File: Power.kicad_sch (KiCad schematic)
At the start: 11 parts

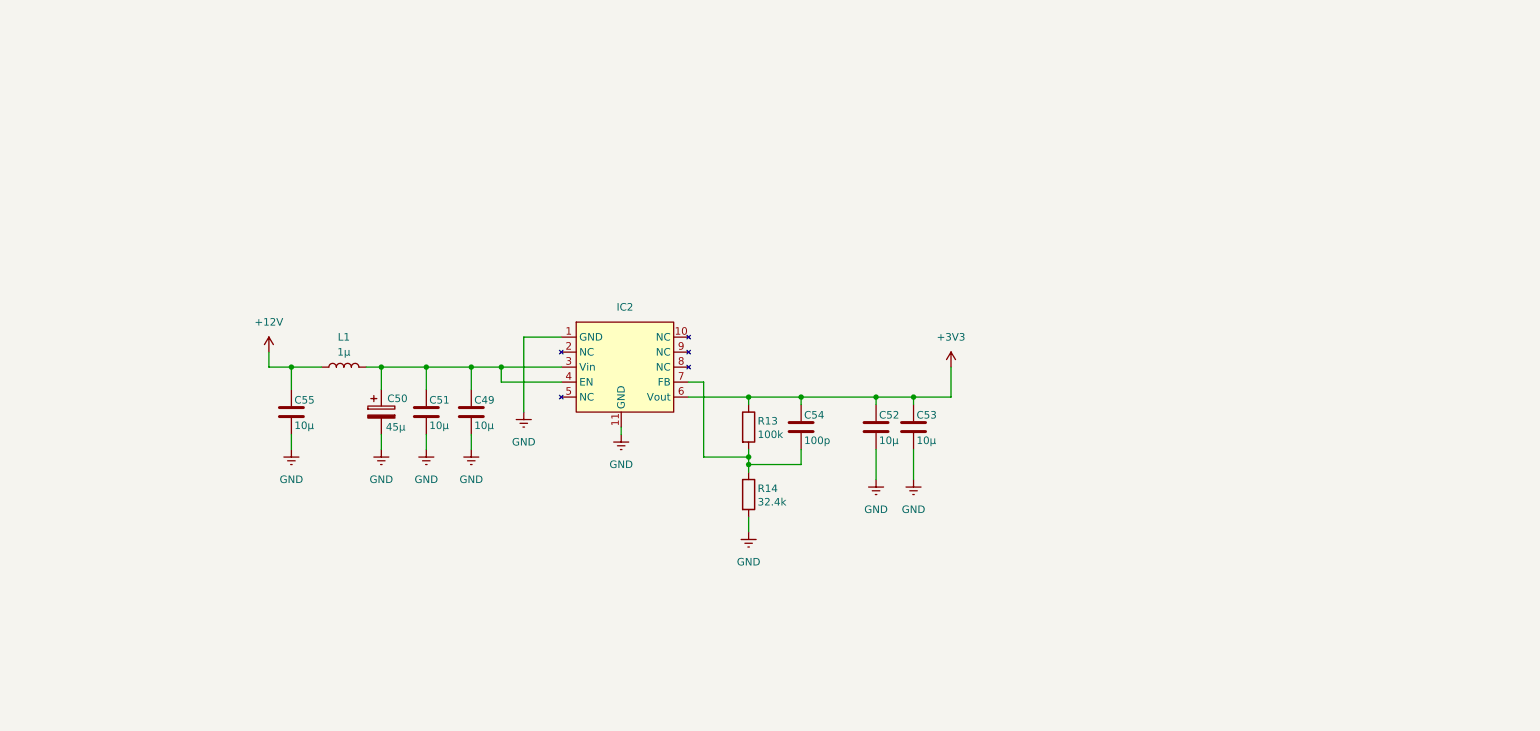
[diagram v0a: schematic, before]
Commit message: power
48V to 12V implemented
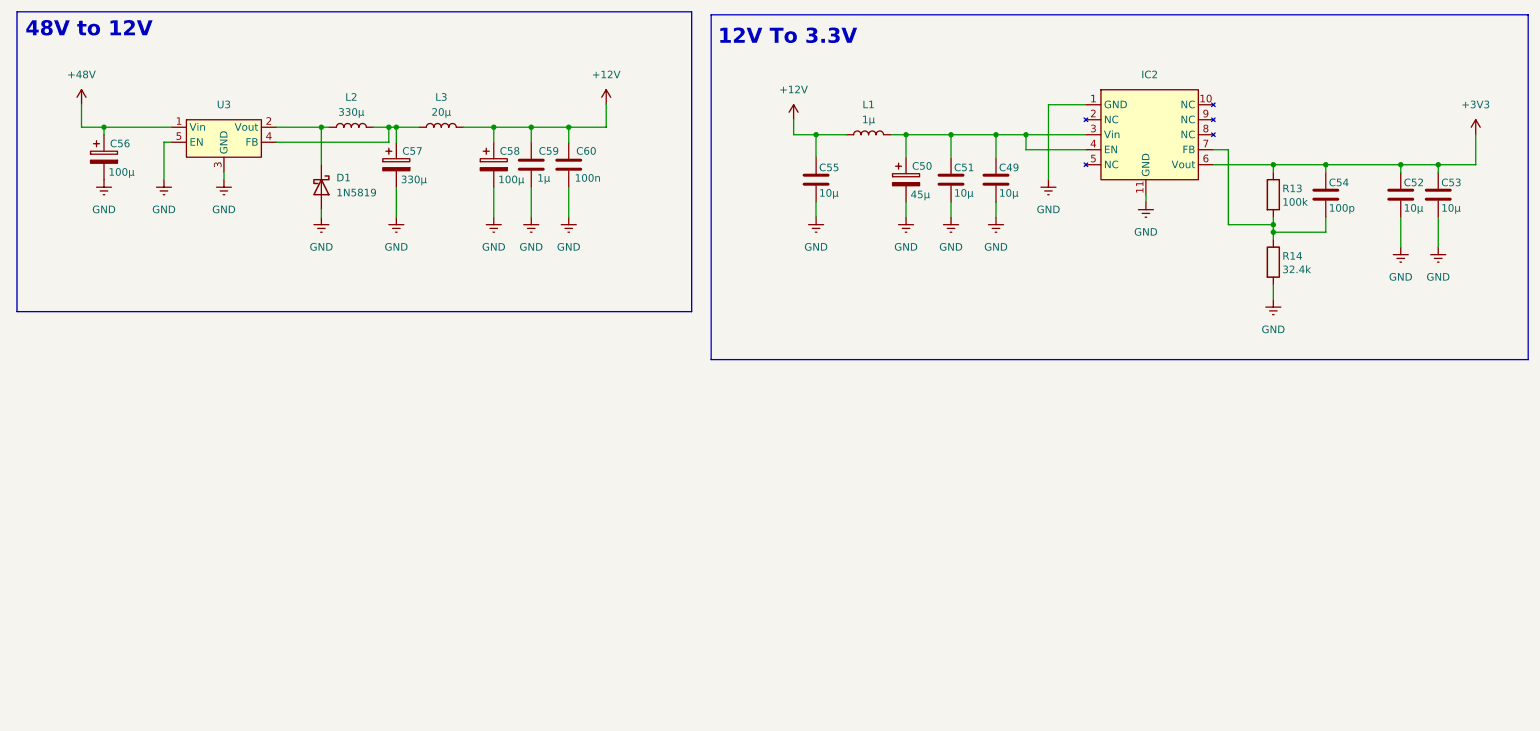
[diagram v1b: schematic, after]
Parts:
- added C56, C58: 100µ, symbol Device:C_Polarized
- added C57: 330µ, symbol Device:C_Polarized
- added C59: 1µ, EEPROM:579-24LC32AFT-ISN, symbol Device:C
- added C60: 100n, EEPROM:579-24LC32AFT-ISN, symbol Device:C
- added D1: 1N5819, Diode_THT:D_DO-41_SOD81_P10.16mm_Horizontal, symbol Diode:1N5819
- added L2: 330µ, symbol Device:L
- added L3: 20µ, symbol Device:L
- added U3: (no value), Footprintsymbolen_samen:TL2575HV-12 (TO-263), symbol Schemasymbolen_samen:TL2575HV-12_(TO-263)
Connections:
- net +12V: now also C58.1, C59.1, C60.1, L3.2
- net GND: now also C56.2, C57.2, C58.2, C59.2, C60.2, D1.2 (A), U3.3 (GND), U3.5 (EN)
- new net: D1.1 (K), L2.1, U3.2 (Vout)
- new net: C57.1, L2.2, L3.1, U3.4 (FB)
- new net +48V: C56.1, U3.1 (Vin)
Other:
- note added: "12V To 3.3V"
- note added: "48V to 12V"
- moved on the sheet: C49, C50, C51, C52, C53, C54, C55, IC2, L1, R13, R14

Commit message: footprints
footprints aan de condensators toegevoegd
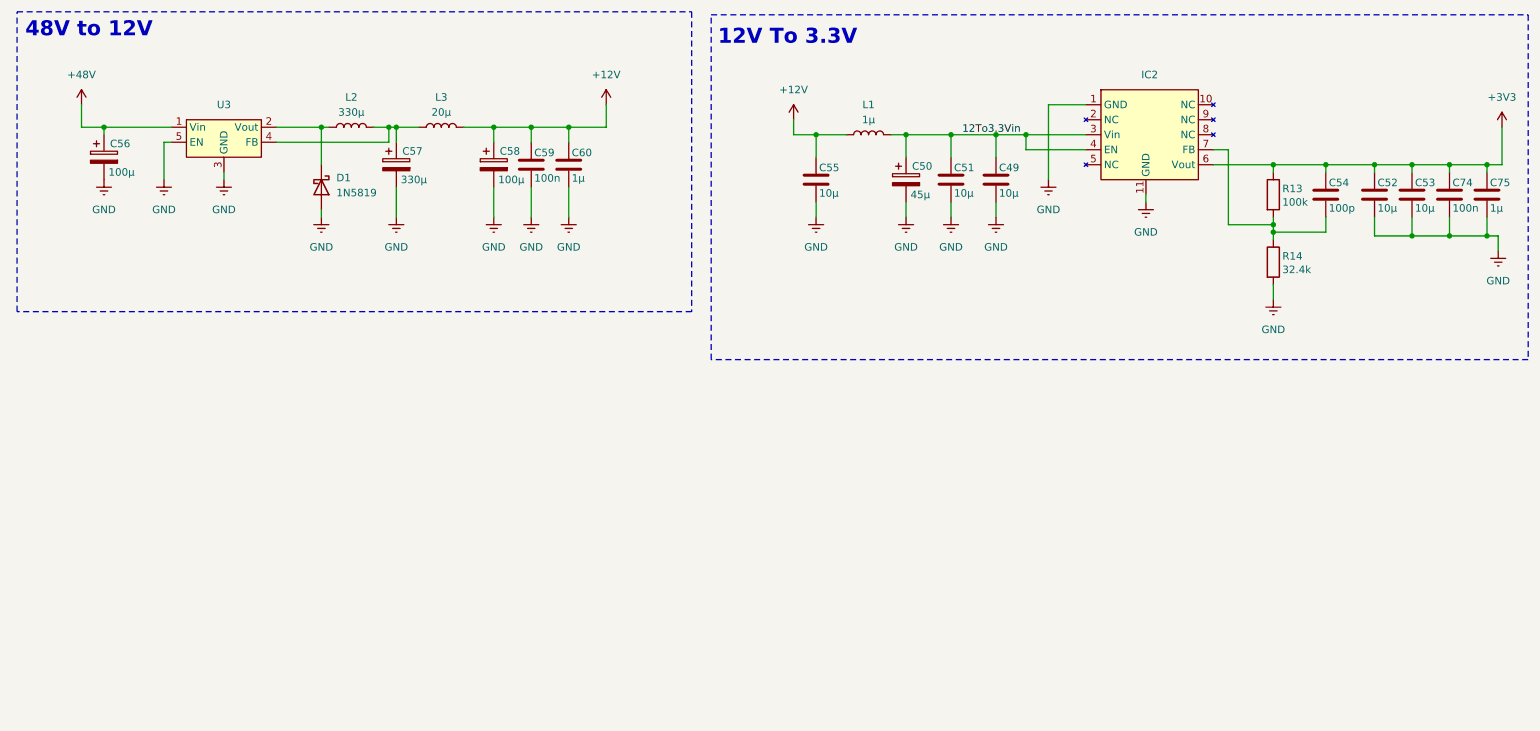
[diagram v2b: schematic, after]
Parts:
- added C74: 100n, Capacitor_SMD:C_0603_1608Metric, symbol Device:C
- added C75: 1µ, Capacitor_SMD:C_0603_1608Metric, symbol Device:C
- C59: value 1µ -> 100n; footprint EEPROM:579-24LC32AFT-ISN -> Capacitor_SMD:C_0603_1608Metric
- C60: value 100n -> 1µ; footprint EEPROM:579-24LC32AFT-ISN -> Capacitor_SMD:C_0603_1608Metric
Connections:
- net +3V3: now also C74.1, C75.1
- net GND: now also C74.2, C75.2
- net 12To3.3Vin: now reaches C49.1, C50.1, C51.1, IC2.3 (Vin), IC2.4 (EN), L1.2
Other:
- moved on the sheet: C52, C53

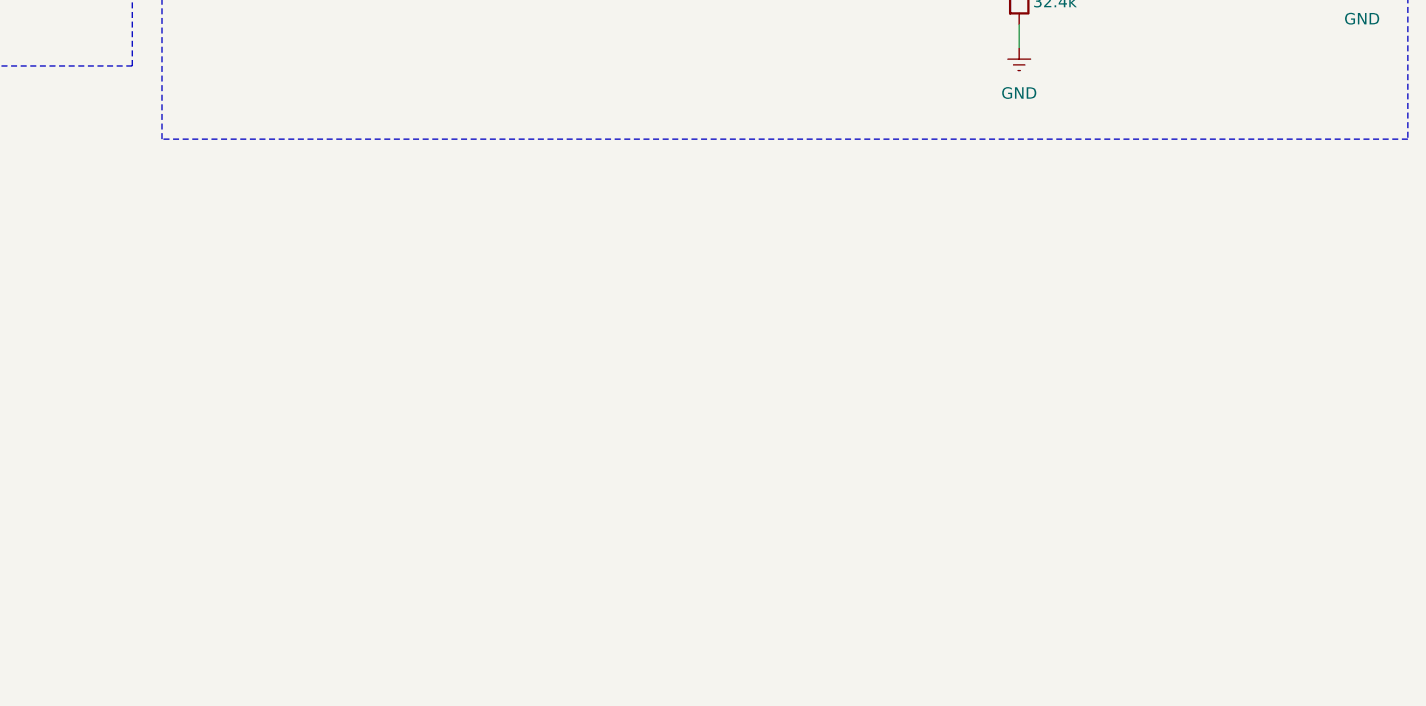
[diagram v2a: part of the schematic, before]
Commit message: BLDC en 5V
bldc motor aangesloten alsook 5V gemaakt
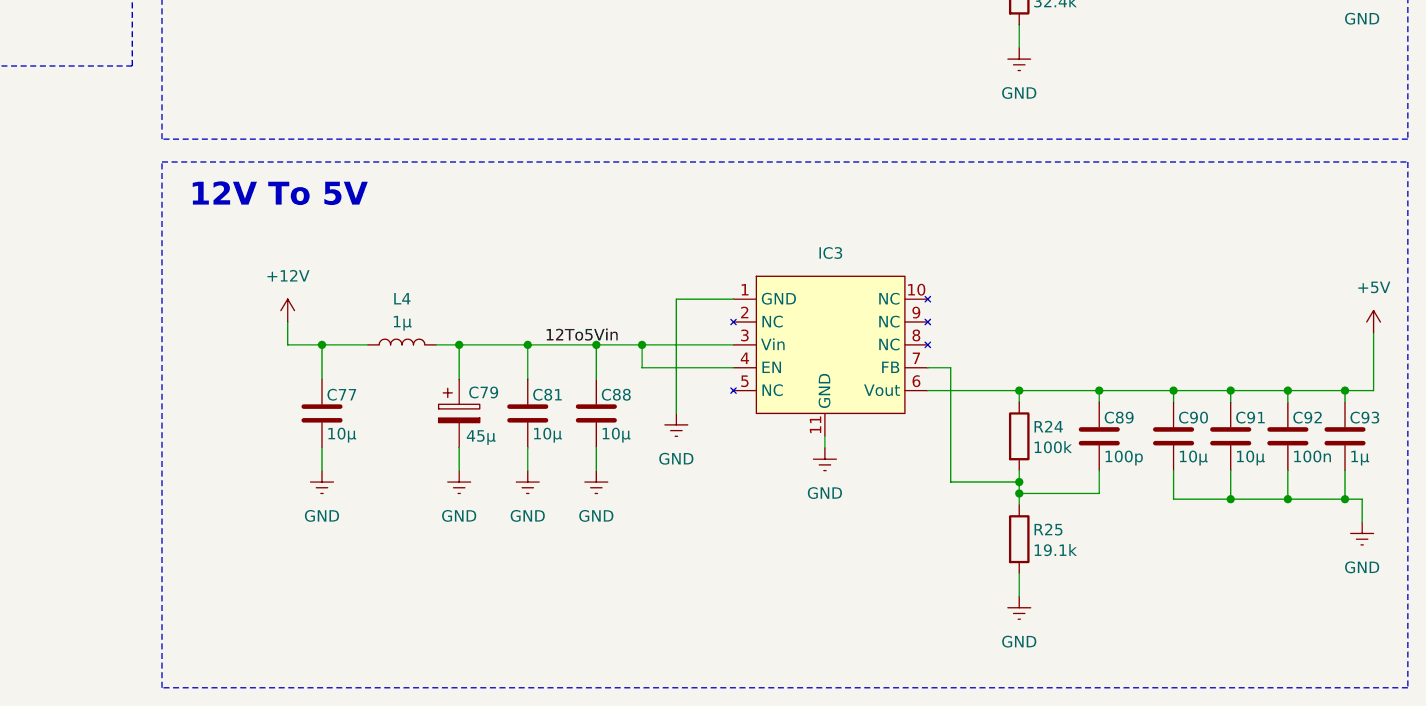
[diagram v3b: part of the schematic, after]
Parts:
- added C77, C81, C88, C90, C91: 10µ, symbol Device:C
- added C79: 45µ, symbol Device:C_Polarized
- added C89: 100p, symbol Device:C
- added C92: 100n, Capacitor_SMD:C_0603_1608Metric, symbol Device:C
- added C93: 1µ, Capacitor_SMD:C_0603_1608Metric, symbol Device:C
- added IC3: (no value), Footprinten_samen:MagI3C Power Module 171013201, symbol Symbolen_samen:MagI3C_Power_Module_171013201
- added L4: 1µ, symbol Device:L
- added R24: 100k, symbol Device:R
- added R25: 19.1k, symbol Device:R
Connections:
- net +12V: now also C77.1, L4.1
- net GND: now also C77.2, C79.2, C81.2, C88.2, C90.2, C91.2, C92.2, C93.2, IC3.1 (GND), IC3.11 (GND), R25.2
- new net: C89.2, IC3.7 (FB), R24.2, R25.1
- new net +5V: C89.1, C90.1, C91.1, C92.1, C93.1, IC3.6 (Vout), R24.1
- new net 12To5Vin: C79.1, C81.1, C88.1, IC3.3 (Vin), IC3.4 (EN), L4.2
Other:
- note added: "12V To 5V"

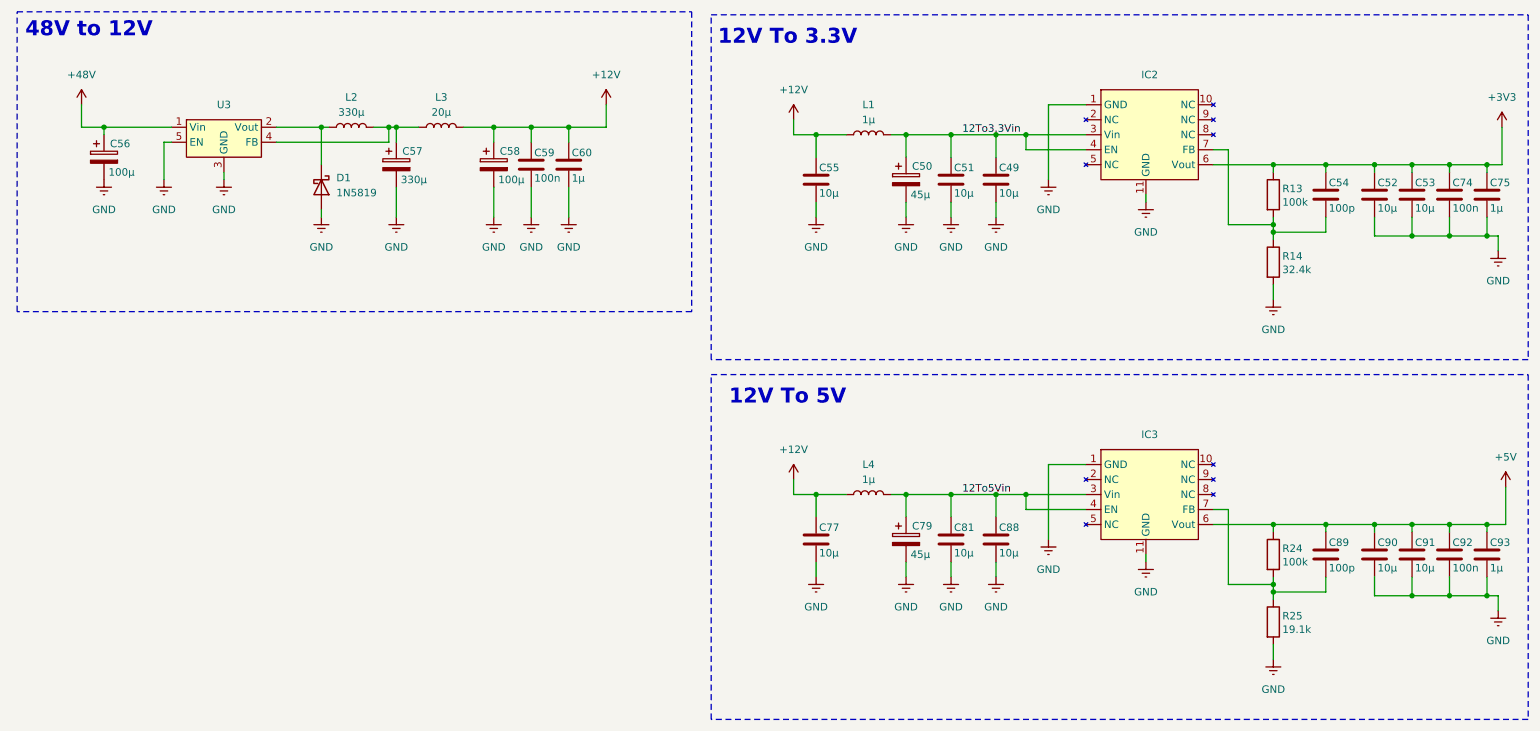
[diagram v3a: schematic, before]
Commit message: schemas klaar
schemas en footprints aan symbolen allemaal juist gemaakt
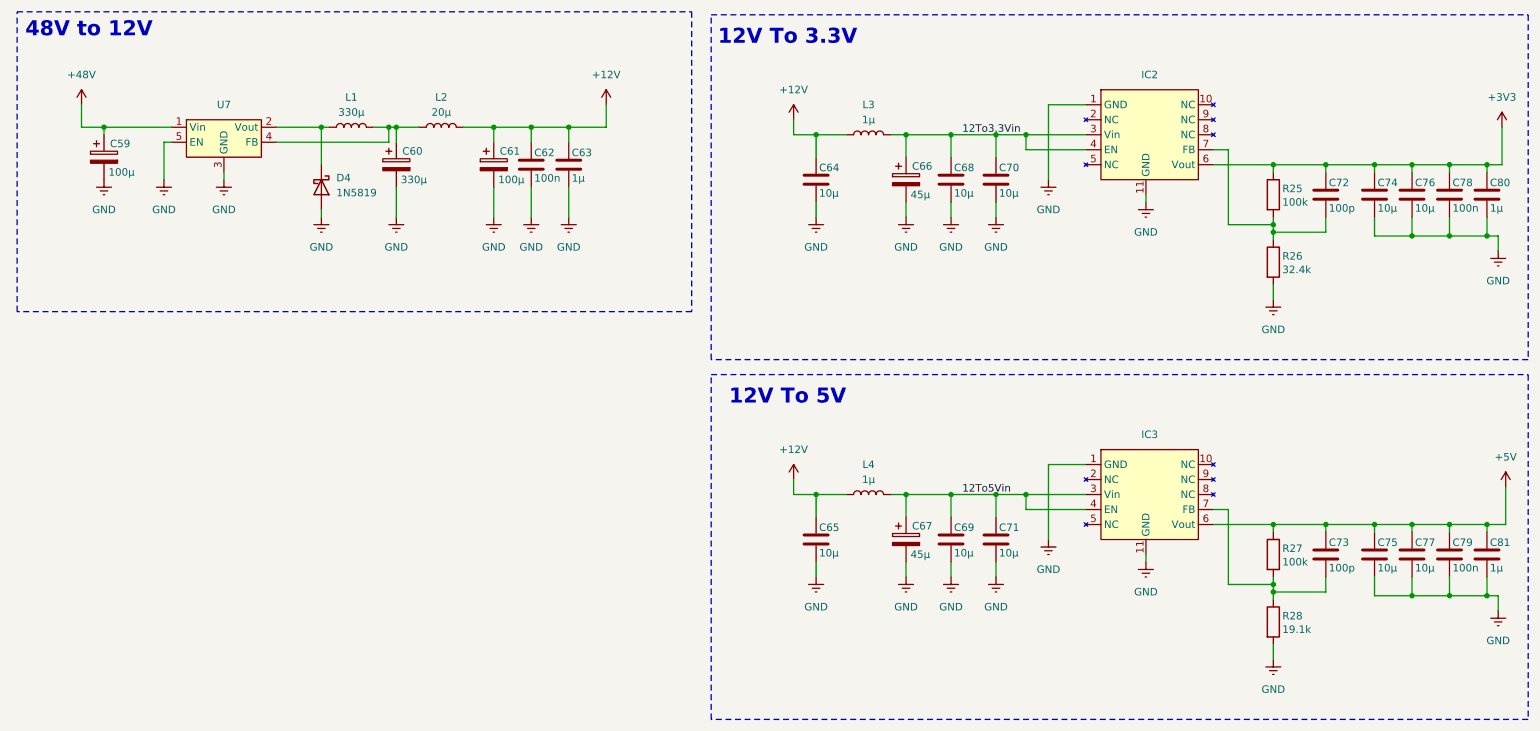
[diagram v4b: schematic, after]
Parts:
- C59: renamed from C56; footprint (none) -> Capacitor_SMD:CP_Elec_10x10.5
- C60: renamed from C57; footprint (none) -> Capacitor_SMD:CP_Elec_10x10.5
- C61: renamed from C58; footprint (none) -> Capacitor_SMD:CP_Elec_8x10.5
- C64: renamed from C55; footprint (none) -> Capacitor_SMD:C_0603_1608Metric
- C65: renamed from C77; footprint (none) -> Capacitor_SMD:C_0603_1608Metric
- C66: renamed from C50; footprint (none) -> Capacitor_SMD:C_0603_1608Metric
- C67: renamed from C79; footprint (none) -> Capacitor_SMD:C_0603_1608Metric
- C68: renamed from C51; footprint (none) -> Capacitor_SMD:C_0603_1608Metric
- C69: renamed from C81; footprint (none) -> Capacitor_SMD:C_0603_1608Metric
- C70: renamed from C49; footprint (none) -> Capacitor_SMD:C_0603_1608Metric
- C71: renamed from C88; footprint (none) -> Capacitor_SMD:C_0603_1608Metric
- C72: renamed from C54; footprint (none) -> Capacitor_SMD:C_0603_1608Metric
- C73: renamed from C89; footprint (none) -> Capacitor_SMD:C_0603_1608Metric
- C74: renamed from C52; footprint (none) -> Capacitor_SMD:C_0603_1608Metric
- C75: renamed from C90; footprint (none) -> Capacitor_SMD:C_0603_1608Metric
- C76: renamed from C53; footprint (none) -> Capacitor_SMD:C_0603_1608Metric
- C77: renamed from C91; footprint (none) -> Capacitor_SMD:C_0603_1608Metric
- IC2, IC3: footprint Footprinten_samen:MagI3C Power Module 171013201 -> Footprintsymbolen_samen:MagI3C Power Module 171013201
- L1: renamed from L2; footprint (none) -> Inductor_SMD:L_APV_ANR3010
- L2: renamed from L3; footprint (none) -> Inductor_SMD:L_APV_ANR3010
- L3: renamed from L1; footprint (none) -> Inductor_SMD_Wurth:L_Wurth_WE-LQSH-2010
- L4: footprint (none) -> Inductor_SMD_Wurth:L_Wurth_WE-LQSH-2010
- R25: renamed from R13; footprint (none) -> Resistor_SMD:R_0603_1608Metric
- R26: renamed from R14; footprint (none) -> Resistor_SMD:R_0603_1608Metric
- R27: renamed from R24; footprint (none) -> Resistor_SMD:R_0603_1608Metric
- R28: renamed from R25; footprint (none) -> Resistor_SMD:R_0603_1608Metric
- renumbered C59 to C62, C60 to C63, C74 to C78, C92 to C79, C75 to C80, C93 to C81, D1 to D4, U3 to U7

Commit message: al de main blokken bij elkaar gezet op juiste plaats
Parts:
- C66, C67: footprint Capacitor_SMD:C_0603_1608Metric -> Capacitor_SMD:CP_Elec_10x10
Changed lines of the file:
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@@
 		)
 	)
+	(label "+12V"
+		(at 152.4 53.34 0)
+		(effects
+			(font
+				(size 1.27 1.27)
+			)
+			(justify left bottom)
+		)
+	)
+	(label "+48V"
+		(at 36.83 52.07 0)
+		(effects
+			(font
+				(size 1.27 1.27)
+			)
+			(justify left bottom)
+		)
+	)
 	(label "12To3.3Vin"
 		(at 177.165 53.34 0)
@@
 		)
 	)
+	(label "+3.3V"
+		(at 231.14 58.42 0)
+		(effects
+			(font
+				(size 1.27 1.27)
+			)
+			(justify left bottom)
+		)
+	)
 	(label "12To5Vin"
 		(at 177.165 114.3 0)
@@
 			)
 		)
-		(property "Footprint" "Capacitor_SMD:C_0603_1608Metric"
+		(property "Footprint" "Capacitor_SMD:CP_Elec_10x10"
 			(at 168.6052 125.73 0)
 			(hide yes)
@@
 			)
 		)
-		(property "Footprint" "Capacitor_SMD:C_0603_1608Metric"
+		(property "Footprint" "Capacitor_SMD:CP_Elec_10x10"
 			(at 168.6052 64.77 0)
 			(hide yes)

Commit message: connector
connector toegevoegd en wat pinnen aangepast
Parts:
- removed D4: 1N5819, Diode_THT:D_DO-41_SOD81_P10.16mm_Horizontal, symbol Diode:1N5819
- added D4: SS210, Diode_SMD:D_SMA, symbol Diode:SS210
- IC2, IC3: value (none) -> MagI3C Power Module 171013201
- U7: value (none) -> TL2575HV-12
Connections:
- net GND: now also D4.2 (A)
- net at L1.1, U7.2 (Vout): now also D4.1 (K)
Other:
- moved on the sheet: C59, C60, C61, C62, C63, L1, L2, U7

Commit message: schema's finalized
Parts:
- added J6: XT60, symbol Connector:Screw_Terminal_01x02
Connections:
- net +48V: now also J6.2 (Pin_2)
- net GND: now also J6.1 (Pin_1)
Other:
- note added: "Power In"
